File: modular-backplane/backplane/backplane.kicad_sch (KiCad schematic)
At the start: 21 parts, among them J1 West, J2 South, J3 North, J4 East, J5 25-E900-02, SW1 A, SW2 B, SW3 C, SW4 D, SW5 E, SW6 F, SW7 G, SW8 H, U1 74HC14, U2 74HC14, U3 VN5E160S

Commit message: Add more part details
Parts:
- J5: Digikey (none) -> 2368-25-E900-02-ND; Manufacturer (none) -> NTE; Mfr. Part # (none) -> 25-E900-02
- R1: Digikey (none) -> RMCF0603JT10K0CT-ND; Manufacturer (none) -> Stackpole; Mfr. Part # (none) -> RMCF0603JT10K0
- U1, U2: Digikey (none) -> 1727-2783-1-ND; Manufacturer (none) -> Nexperia; Mfr. Part # (none) -> 74HC14D,653
- U3: Digikey (none) -> 497-18886-1-ND; Manufacturer (none) -> STMicroelectronics; Mfr. Part # (none) -> VN5E160STR-E
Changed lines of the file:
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@@
+      (effects (font (size 1.27 1.27)) hide)
+    )
+    (property "Digikey" "1727-2783-1-ND " (id 4) (at 556.26 111.76 0)
+      (effects (font (size 1.27 1.27)) hide)
+    )
+    (property "Manufacturer" "Nexperia" (id 5) (at 556.26 111.76 0)
+      (effects (font (size 1.27 1.27)) hide)
+    )
+    (property "Mfr. Part #" "74HC14D,653" (id 6) (at 556.26 111.76 0)
       (effects (font (size 1.27 1.27)) hide)
     )
@@
       (effects (font (size 1.27 1.27)) hide)
     )
+    (property "Digikey" "1727-2783-1-ND " (id 4) (at 533.4 81.28 0)
+      (effects (font (size 1.27 1.27)) hide)
+    )
+    (property "Manufacturer" "Nexperia" (id 5) (at 533.4 81.28 0)
+      (effects (font (size 1.27 1.27)) hide)
+    )
+    (property "Mfr. Part #" "74HC14D,653" (id 6) (at 533.4 81.28 0)
+      (effects (font (size 1.27 1.27)) hide)
+    )
     (pin "1")
     (pin "2")
@@
       (effects (font (size 1.27 1.27)) hide)
     )
+    (property "Digikey" "1727-2783-1-ND " (id 4) (at 556.26 127 0)
+      (effects (font (size 1.27 1.27)) hide)
+    )
+    (property "Manufacturer" "Nexperia" (id 5) (at 556.26 127 0)
+      (effects (font (size 1.27 1.27)) hide)
+    )
+    (property "Mfr. Part #" "74HC14D,653" (id 6) (at 556.26 127 0)
+      (effects (font (size 1.27 1.27)) hide)
+    )
     (pin "1")
     (pin "2")
@@
       (effects (font (size 1.27 1.27)) hide)
     )
+    (property "Digikey" "1727-2783-1-ND " (id 4) (at 556.26 81.28 0)
+      (effects (font (size 1.27 1.27)) hide)
+    )
+    (property "Manufacturer" "Nexperia" (id 5) (at 556.26 81.28 0)
+      (effects (font (size 1.27 1.27)) hide)
+    )
+    (property "Mfr. Part #" "74HC14D,653" (id 6) (at 556.26 81.28 0)
+      (effects (font (size 1.27 1.27)) hide)
+    )
     (pin "1")
     (pin "2")
@@
     )
     (property "Datasheet" "~" (id 3) (at 455.93 175.26 0)
+      (effects (font (size 1.27 1.27)) hide)
+    )
+    (property "Digikey" "2368-25-E900-02-ND" (id 4) (at 455.93 175.26 0)
+      (effects (font (size 1.27 1.27)) hide)
+    )
+    (property "Manufacturer" "NTE" (id 5) (at 455.93 175.26 0)
+      (effects (font (size 1.27 1.27)) hide)
+    )
+    (property "Mfr. Part #" "25-E900-02" (id 6) (at 455.93 175.26 0)
       (effects (font (size 1.27 1.27)) hide)
     )
@@
       (effects (font (size 1.27 1.27)) hide)
     )
+    (property "Digikey" "RMCF0603JT10K0CT-ND" (id 4) (at 455.93 234.95 0)
+      (effects (font (size 1.27 1.27)) hide)
+    )
+    (property "Manufacturer" "Stackpole" (id 5) (at 455.93 234.95 0)
+      (effects (font (size 1.27 1.27)) hide)
+    )
+    (property "Mfr. Part #" "RMCF0603JT10K0" (id 6) (at 455.93 234.95 0)
+      (effects (font (size 1.27 1.27)) hide)
+    )
     (pin "1")
     (pin "2")
@@
       (effects (font (size 1.27 1.27)) hide)
     )
+    (property "Digikey" "1727-2783-1-ND " (id 4) (at 556.26 172.72 0)
+      (effects (font (size 1.27 1.27)) hide)
+    )
+    (property "Manufacturer" "Nexperia" (id 5) (at 556.26 172.72 0)
+      (effects (font (size 1.27 1.27)) hide)
+    )
+    (property "Mfr. Part #" "74HC14D,653" (id 6) (at 556.26 172.72 0)
+      (effects (font (size 1.27 1.27)) hide)
+    )
     (pin "1")
     (pin "2")
@@
       (effects (font (size 1.27 1.27)) hide)
     )
+    (property "Digikey" "1727-2783-1-ND " (id 4) (at 556.26 187.96 0)
+      (effects (font (size 1.27 1.27)) hide)
+    )
+    (property "Manufacturer" "Nexperia" (id 5) (at 556.26 187.96 0)
+      (effects (font (size 1.27 1.27)) hide)
+    )
+    (property "Mfr. Part #" "74HC14D,653" (id 6) (at 556.26 187.96 0)
+      (effects (font (size 1.27 1.27)) hide)
+    )
     (pin "1")
     (pin "2")
@@
     )
     (property "Datasheet" "http://www.ti.com/lit/gpn/sn74HC14" (id 3) (at 528.32 151.13 0)
+      (effects (font (size 1.27 1.27)) hide)
+    )
+    (property "Digikey" "1727-2783-1-ND " (id 4) (at 528.32 151.13 0)
+      (effects (font (size 1.27 1.27)) hide)
+    )
+    (property "Manufacturer" "Nexperia" (id 5) (at 528.32 151.13 0)
+      (effects (font (size 1.27 1.27)) hide)
+    )
+    (property "Mfr. Part #" "74HC14D,653" (id 6) (at 528.32 151.13 0)
       (effects (font (size 1.27 1.27)) hide)
     )
@@
     )
     (property "Datasheet" "http://www.ti.com/lit/gpn/sn74HC14" (id 3) (at 556.26 96.52 0)
+      (effects (font (size 1.27 1.27)) hide)
+    )
+    (property "Digikey" "1727-2783-1-ND " (id 4) (at 556.26 96.52 0)
+      (effects (font (size 1.27 1.27)) hide)
+    )
+    (property "Manufacturer" "Nexperia" (id 5) (at 556.26 96.52 0)
+      (effects (font (size 1.27 1.27)) hide)
+    )
+    (property "Mfr. Part #" "74HC14D,653" (id 6) (at 556.26 96.52 0)
       (effects (font (size 1.27 1.27)) hide)
     )
@@
       (effects (font (size 1.27 1.27)) hide)
     )
+    (property "Digikey" "497-18886-1-ND" (id 4) (at 472.44 243.84 0)
+      (effects (font (size 1.27 1.27)) hide)
+    )
+    (property "Manufacturer" "STMicroelectronics" (id 5) (at 472.44 243.84 0)
+      (effects (font (size 1.27 1.27)) hide)
+    )
+    (property "Mfr. Part #" "VN5E160STR-E" (id 6) (at 472.44 243.84 0)
+      (effects (font (size 1.27 1.27)) hide)
+    )
     (pin "1")
     (pin "2")
@@
       (effects (font (size 1.27 1.27)) hide)
     )
+    (property "Digikey" "1727-2783-1-ND " (id 4) (at 556.26 142.24 0)
+      (effects (font (size 1.27 1.27)) hide)
+    )
+    (property "Manufacturer" "Nexperia" (id 5) (at 556.26 142.24 0)
+      (effects (font (size 1.27 1.27)) hide)
+    )
+    (property "Mfr. Part #" "74HC14D,653" (id 6) (at 556.26 142.24 0)
+      (effects (font (size 1.27 1.27)) hide)
+    )
     (pin "1")
     (pin "2")
@@
     )
     (property "Datasheet" "http://www.ti.com/lit/gpn/sn74HC14" (id 3) (at 528.32 107.95 0)
+      (effects (font (size 1.27 1.27)) hide)
+    )
+    (property "Digikey" "1727-2783-1-ND " (id 4) (at 528.32 107.95 0)
+      (effects (font (size 1.27 1.27)) hide)
+    )
+    (property "Manufacturer" "Nexperia" (id 5) (at 528.32 107.95 0)
+      (effects (font (size 1.27 1.27)) hide)
+    )
+    (property "Mfr. Part #" "74HC14D,653" (id 6) (at 528.32 107.95 0)
       (effects (font (size 1.27 1.27)) hide)
     )
@@
       (effects (font (size 1.27 1.27)) hide)
     )
+    (property "Digikey" "1727-2783-1-ND " (id 4) (at 556.26 157.48 0)
+      (effects (font (size 1.27 1.27)) hide)
+    )
+    (property "Manufacturer" "Nexperia" (id 5) (at 556.26 157.48 0)
+      (effects (font (size 1.27 1.27)) hide)
+    )
+    (property "Mfr. Part #" "74HC14D,653" (id 6) (at 556.26 157.48 0)
+      (effects (font (size 1.27 1.27)) hide)
+    )

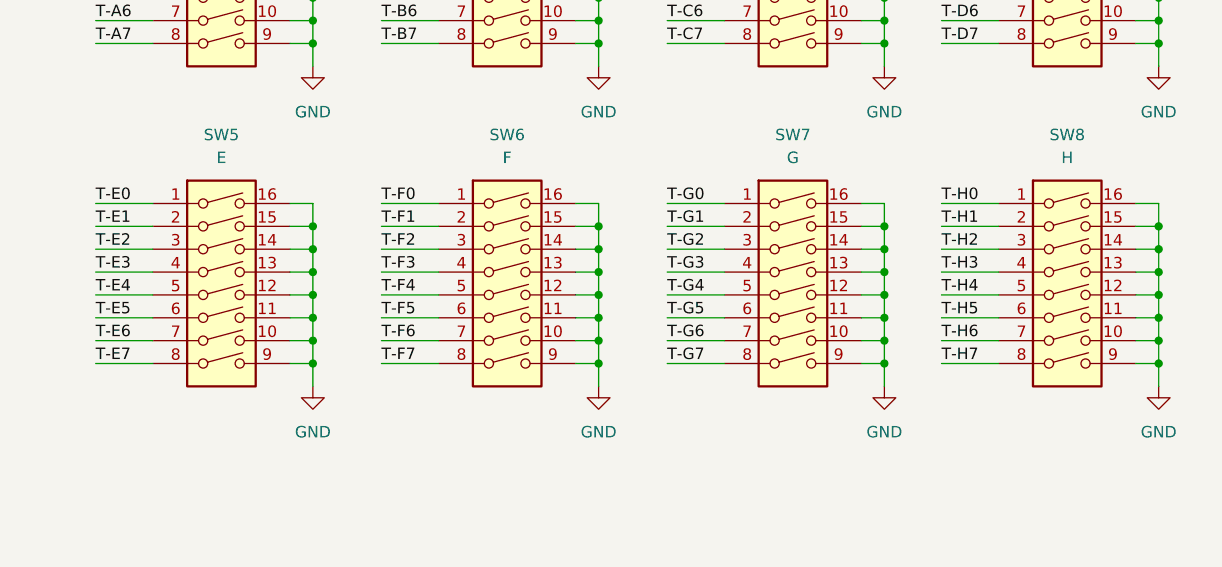
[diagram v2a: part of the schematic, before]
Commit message: Place and route DIP switches
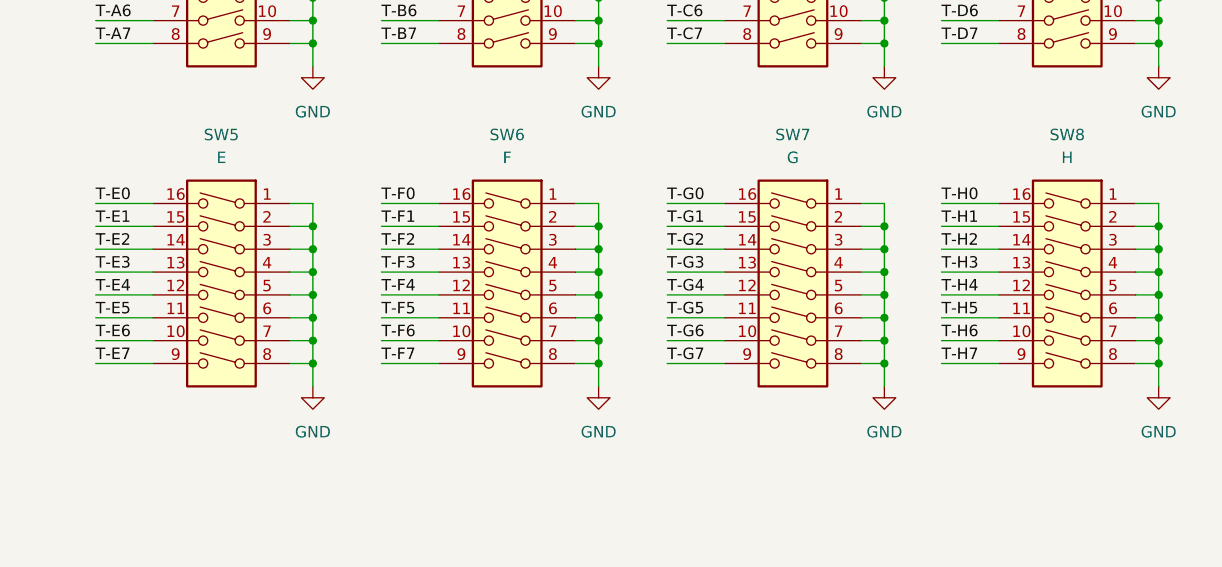
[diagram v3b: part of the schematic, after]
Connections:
- net GND: now also SW5.1, SW5.2, SW5.3, SW5.4, SW5.5, SW5.6, SW5.7, SW5.8, SW6.1, SW6.2, SW6.3, SW6.4, SW6.5, SW6.6, SW6.7, SW6.8, SW7.1, SW7.2, SW7.3, SW7.4, SW7.5, SW7.6, SW7.7, SW7.8, SW8.1, SW8.2, SW8.3, SW8.4, SW8.5, SW8.6, SW8.7, SW8.8; no longer SW5.10, SW5.11, SW5.12, SW5.13, SW5.14, SW5.15, SW5.16, SW5.9, SW6.10, SW6.11, SW6.12, SW6.13, SW6.14, SW6.15, SW6.16, SW6.9, SW7.10, SW7.11, SW7.12, SW7.13, SW7.14, SW7.15, SW7.16, SW7.9, SW8.10, SW8.11, SW8.12, SW8.13, SW8.14, SW8.15, SW8.16, SW8.9
- net T-E0: now also SW5.16; no longer SW5.1
- net T-E1: now also SW5.15; no longer SW5.2
- net T-E2: now also SW5.14; no longer SW5.3
- net T-E3: now also SW5.13; no longer SW5.4
- net T-E4: now also SW5.12; no longer SW5.5
- net T-E5: now also SW5.11; no longer SW5.6
- net T-E6: now also SW5.10; no longer SW5.7
- net T-E7: now also SW5.9; no longer SW5.8
- net T-F0: now also SW6.16; no longer SW6.1
- net T-F1: now also SW6.15; no longer SW6.2
- net T-F2: now also SW6.14; no longer SW6.3
- net T-F3: now also SW6.13; no longer SW6.4
- net T-F4: now also SW6.12; no longer SW6.5
- net T-F5: now also SW6.11; no longer SW6.6
- net T-F6: now also SW6.10; no longer SW6.7
- net T-F7: now also SW6.9; no longer SW6.8
- net T-G0: now also SW7.16; no longer SW7.1
- net T-G1: now also SW7.15; no longer SW7.2
- net T-G2: now also SW7.14; no longer SW7.3
- net T-G3: now also SW7.13; no longer SW7.4
- net T-G4: now also SW7.12; no longer SW7.5
- net T-G5: now also SW7.11; no longer SW7.6
- net T-G6: now also SW7.10; no longer SW7.7
- net T-G7: now also SW7.9; no longer SW7.8
- net T-H0: now also SW8.16; no longer SW8.1
- net T-H1: now also SW8.15; no longer SW8.2
- net T-H2: now also SW8.14; no longer SW8.3
- net T-H3: now also SW8.13; no longer SW8.4
- net T-H4: now also SW8.12; no longer SW8.5
- net T-H5: now also SW8.11; no longer SW8.6
- net T-H6: now also SW8.10; no longer SW8.7
- net T-H7: now also SW8.9; no longer SW8.8
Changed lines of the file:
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@@
     )
   )
-  (symbol (lib_id "Switch:SW_DIP_x08") (at 462.28 341.63 0) (unit 1)
+  (symbol (lib_id "Switch:SW_DIP_x08") (at 462.28 341.63 0) (mirror y) (unit 1)
     (in_bom yes) (on_board yes) (fields_autoplaced)
     (property "Reference" "SW5" (id 0) (at 462.28 323.85 0))
@@
     )
   )
-  (symbol (lib_id "Switch:SW_DIP_x08") (at 494.03 341.63 0) (unit 1)
+  (symbol (lib_id "Switch:SW_DIP_x08") (at 494.03 341.63 0) (mirror y) (unit 1)
     (in_bom yes) (on_board yes) (fields_autoplaced)
     (property "Reference" "SW6" (id 0) (at 494.03 323.85 0))
@@
     (pin "9")
   )
-  (symbol (lib_id "Switch:SW_DIP_x08") (at 525.78 341.63 0) (unit 1)
+  (symbol (lib_id "Switch:SW_DIP_x08") (at 525.78 341.63 0) (mirror y) (unit 1)
     (in_bom yes) (on_board yes) (fields_autoplaced)
     (property "Reference" "SW7" (id 0) (at 525.78 323.85 0))
@@
     (pin "9")
   )
-  (symbol (lib_id "Switch:SW_DIP_x08") (at 556.26 341.63 0) (unit 1)
+  (symbol (lib_id "Switch:SW_DIP_x08") (at 556.26 341.63 0) (mirror y) (unit 1)
     (in_bom yes) (on_board yes) (fields_autoplaced)
     (property "Reference" "SW8" (id 0) (at 556.26 323.85 0))

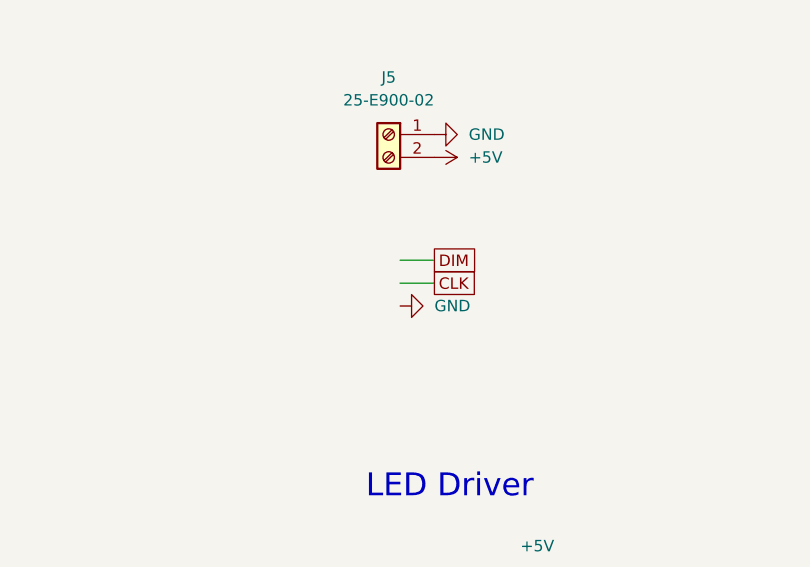
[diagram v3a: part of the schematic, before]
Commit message: Place and route power/management connectors and power switch
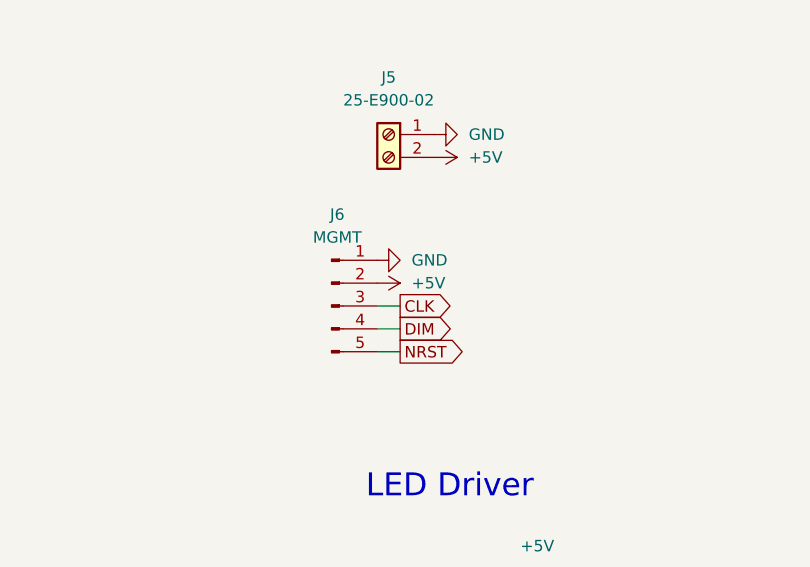
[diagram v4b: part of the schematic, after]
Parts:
- added J6: MGMT, Connector_PinHeader_2.54mm:PinHeader_1x05_P2.54mm_Vertical_SMD_Pin1Right, symbol Connector:Conn_01x05_Male
- J5: footprint (none) -> agausmann:Conn_NTE_25-E900-02_01x02_P5.00mm_Vertical
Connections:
- net +5V: now also J6.2 (Pin_2)
- net CLK: now also J6.3 (Pin_3)
- net DIM: now also J6.4 (Pin_4)
- net GND: now also J6.1 (Pin_1)
- new net NRST: J6.5 (Pin_5)
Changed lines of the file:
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@@
     (stroke (width 0) (type default) (color 0 0 0 0))
   )
-  (wire (pts (xy 461.01 189.23) (xy 457.2 189.23))
+  (wire (pts (xy 457.2 196.85) (xy 454.66 196.85))
     (stroke (width 0) (type default) (color 0 0 0 0))
   )
@@
     (stroke (width 0) (type default) (color 0 0 0 0))
   )
-  (wire (pts (xy 461.01 191.77) (xy 457.2 191.77))
+  (wire (pts (xy 457.2 194.31) (xy 454.66 194.31))
     (stroke (width 0) (type default) (color 0 0 0 0))
   )
@@
     (stroke (width 0) (type default) (color 0 0 0 0))
   )
+  (wire (pts (xy 454.66 199.39) (xy 457.2 199.39))
+    (stroke (width 0) (type default) (color 0 0 0 0))
+  )
   (wire (pts (xy 187.96 137.16) (xy 189.23 137.16))
     (stroke (width 0) (type default) (color 0 0 0 0))
@@
     )
   )
-  (global_label "DIM" (shape passive) (at 461.01 189.23 0) (fields_autoplaced)
+  (global_label "DIM" (shape output) (at 457.2 196.85 0) (fields_autoplaced)
     (effects (font (size 1.27 1.27)) (justify left))
-    (property "Intersheet References" "${INTERSHEET_REFS}" (id 0) (at 466.7493 189.1506 0)
+    (property "Intersheet References" "${INTERSHEET_REFS}" (id 0) (at 462.9393 196.7706 0)
       (effects (font (size 1.27 1.27)) (justify left) hide)
     )
@@
     )
   )
-  (global_label "CLK" (shape passive) (at 461.01 191.77 0) (fields_autoplaced)
+  (global_label "NRST" (shape output) (at 457.2 199.39 0) (fields_autoplaced)
     (effects (font (size 1.27 1.27)) (justify left))
-    (property "Intersheet References" "${INTERSHEET_REFS}" (id 0) (at 466.9912 191.6906 0)
+    (property "Intersheet References" "${INTERSHEET_REFS}" (id 0) (at 464.3907 199.3106 0)
+      (effects (font (size 1.27 1.27)) (justify left) hide)
+    )
+  )
+  (global_label "CLK" (shape output) (at 457.2 194.31 0) (fields_autoplaced)
+    (effects (font (size 1.27 1.27)) (justify left))
+    (property "Intersheet References" "${INTERSHEET_REFS}" (id 0) (at 463.1812 194.2306 0)
       (effects (font (size 1.27 1.27)) (justify left) hide)
     )
@@
     (pin "1")
   )
+  (symbol (lib_id "Connector:Conn_01x05_Male") (at 449.58 194.31 0) (unit 1)
+    (in_bom yes) (on_board yes) (fields_autoplaced)
+    (property "Reference" "J6" (id 0) (at 450.215 184.15 0))
+    (property "Value" "MGMT" (id 1) (at 450.215 186.69 0))
+    (property "Footprint" "Connector_PinHeader_2.54mm:PinHeader_1x05_P2.54mm_Vertical_SMD_Pin1Right" (id 2) (at 449.58 194.31 0)
+      (effects (font (size 1.27 1.27)) hide)
+    )
+    (property "Datasheet" "~" (id 3) (at 449.58 194.31 0)
+      (effects (font (size 1.27 1.27)) hide)
+    )
+    (property "Digikey" "10129380-905002BLF-ND" (id 4) (at 449.58 194.31 0)
+      (effects (font (size 1.27 1.27)) hide)
+    )
+    (property "Manufacturer" "Amphenol ICC" (id 5) (at 449.58 194.31 0)
+      (effects (font (size 1.27 1.27)) hide)
+    )
+    (property "Mfr. Part #" "10129380-905002BLF" (id 6) (at 449.58 194.31 0)
+      (effects (font (size 1.27 1.27)) hide)
+    )
+    (pin "1")
+    (pin "2")
+    (pin "3")
+    (pin "4")
+    (pin "5")
+  )
   (symbol (lib_id "power:GND") (at 504.19 316.23 0) (unit 1)
     (in_bom yes) (on_board yes) (fields_autoplaced)
@@
     (pin "9")
   )
-  (symbol (lib_id "power:GND") (at 457.2 194.31 90) (unit 1)
+  (symbol (lib_id "power:GND") (at 454.66 189.23 90) (unit 1)
     (in_bom yes) (on_board yes) (fields_autoplaced)
-    (property "Reference" "#PWR0113" (id 0) (at 463.55 194.31 0)
+    (property "Reference" "#PWR0113" (id 0) (at 461.01 189.23 0)
       (effects (font (size 1.27 1.27)) hide)
     )
-    (property "Value" "GND" (id 1) (at 461.01 194.3099 90)
+    (property "Value" "GND" (id 1) (at 458.47 189.2299 90)
       (effects (font (size 1.27 1.27)) (justify right))
     )
-    (property "Footprint" "" (id 2) (at 457.2 194.31 0)
+    (property "Footprint" "" (id 2) (at 454.66 189.23 0)
       (effects (font (size 1.27 1.27)) hide)
     )
-    (property "Datasheet" "" (id 3) (at 457.2 194.31 0)
+    (property "Datasheet" "" (id 3) (at 454.66 189.23 0)
       (effects (font (size 1.27 1.27)) hide)
     )
@@
     (property "Reference" "J5" (id 0) (at 455.93 168.91 0))
     (property "Value" "25-E900-02" (id 1) (at 455.93 171.45 0))
-    (property "Footprint" "" (id 2) (at 455.93 175.26 0)
+    (property "Footprint" "agausmann:Conn_NTE_25-E900-02_01x02_P5.00mm_Vertical" (id 2) (at 455.93 175.26 0)
       (effects (font (size 1.27 1.27)) hide)
     )
@@
     (pin "7")
   )
+  (symbol (lib_id "power:+5V") (at 454.66 191.77 270) (unit 1)
+    (in_bom yes) (on_board yes) (fields_autoplaced)
+    (property "Reference" "#PWR0212" (id 0) (at 450.85 191.77 0)
+      (effects (font (size 1.27 1.27)) hide)
+    )
+    (property "Value" "+5V" (id 1) (at 458.47 191.7699 90)
+      (effects (font (size 1.27 1.27)) (justify left))
+    )
+    (property "Footprint" "" (id 2) (at 454.66 191.77 0)
+      (effects (font (size 1.27 1.27)) hide)
+    )
+    (property "Datasheet" "" (id 3) (at 454.66 191.77 0)
+      (effects (font (size 1.27 1.27)) hide)
+    )
+    (pin "1")
+  )
   (symbol (lib_id "Connector_Generic:Conn_01x24") (at 412.75 101.6 0) (unit 1)
     (in_bom yes) (on_board yes) (fields_autoplaced)
@@
       (reference "#PWR0211") (unit 1) (value "+5V") (footprint "")
     )
+    (path "/f00e7bf2-0bfe-4555-9cf9-bf34ecadf013"
+      (reference "#PWR0212") (unit 1) (value "+5V") (footprint "")
+    )
     (path "/852e5412-4b34-47d4-9b60-8d540a352e29"
       (reference "H1") (unit 1) (value "MountingHole") (footprint "MountingHole:MountingHole_2.2mm_M2_Pad")
@@
     )
     (path "/8b7c65d7-245a-4460-9db5-be8fd53981c7"
-      (reference "J5") (unit 1) (value "25-E900-02") (footprint "")
+      (reference "J5") (unit 1) (value "25-E900-02") (footprint "agausmann:Conn_NTE_25-E900-02_01x02_P5.00mm_Vertical")
+    )
+    (path "/57f0aa0f-9b8a-4c37-aa3c-aece509b562a"
+      (reference "J6") (unit 1) (value "MGMT") (footprint "Connector_PinHeader_2.54mm:PinHeader_1x05_P2.54mm_Vertical_SMD_Pin1Right")
     )
     (path "/ebdf8072-9546-4a33-8910-8477456421e3/a39da481-1141-42de-86a9-064e8c57c993"

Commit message: Place and route clock tree; remove NRST from management header
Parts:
- added unit 3 of U1
- added unit 3 of U2
- added unit 2 of U2
- J6: footprint Connector_PinHeader_2.54mm:PinHeader_1x05_P2.54mm_Vertical_SMD_Pin1Right -> Connector_PinHeader_2.54mm:PinHeader_1x04_P2.54mm_Vertical_SMD_Pin1Right; symbol Connector:Conn_01x05_Male -> Connector:Conn_01x04_Male; Digikey 10129380-905002BLF-ND -> 10129380-904002BLF-ND; Mfr. Part # 10129380-905002BLF -> 10129380-904002BLF
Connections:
- net CLK: now also U1.9; no longer U1.1
- net CLK0: now also U1.4; no longer U1.4
- net CLK1: now also U1.12; no longer U1.6
- net CLK2: now also U1.10; no longer U1.8
- net CLK3: now also U1.2; no longer U1.10
- net CLK4: now also U2.10; no longer U2.2
- net CLK5: now also U2.8; no longer U2.4
- net CLK6: now also U2.12; no longer U2.6
- net CLK7: now also U2.2; no longer U2.8
- net GND: now also U1.5, U2.3, U2.5
- removed net NRST: J6.5 (Pin_5)
- new net: U1.1, U1.11, U1.13, U1.3, U1.8, U2.1, U2.11, U2.13, U2.9
- no-connect marks 62 -> 65
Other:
- note added: "Clock Tree"
- note removed: "Clock Distribution"
- moved on the sheet: U1B, U1F
